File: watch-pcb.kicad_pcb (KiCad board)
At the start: 4 copper layers, 40 x 42 mm, 134 parts, among them J4 USB_C_Receptacle, J5 ESP_ANT, J6 GPS_ANT, Q1 BC818, U1 LIS3MDL, U10 MX25LM51245GXDI00, U11 LSM6DSV16XTR, U3 DRV2605LYZFR, U4 TPS63001, U5 AP131-18, U6 MAX30102, U7 MCP73871-2AA, U8 ESP32-S3, U9 S80KS5123GABHI020, Y1 40MHz(10ppm), Y2 32.768kHz

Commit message: custom symbols moar
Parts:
- moved U11 5.92 mm to (90.2, 104.8), turned to 0 degrees
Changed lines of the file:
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@@
   )
   (footprint "LSM6DSV16XTR:LGA14L_LSM6_STM" (layer "F.Cu")
-    (at 84.35 104.3 90)
+    (at 90.249811 104.8189)
     (tags "LSM6DSV16XTR ")
     (property "Sheetfile" "watch_pcb.kicad_sch")
@@
     (property "ki_keywords" "LSM6DSV16XTR")
     (attr smd)
-    (fp_text reference "U11" (at 0 2.550189 90 unlocked) (layer "F.SilkS")
-        (effects (font (size 1 1) (thickness 0.15)))
-    )
-    (fp_text value "LSM6DSV16XTR" (at 0 0 90 unlocked) (layer "F.Fab")
-        (effects (font (size 1 1) (thickness 0.15)))
-    )
-    (fp_text user "*" (at -2.0828 -0.750189 90 unlocked) (layer "F.SilkS")
-        (effects (font (size 1 1) (thickness 0.15)))
-    )
-    (fp_text user "*" (at -2.0828 -0.750189 90) (layer "F.SilkS")
-        (effects (font (size 1 1) (thickness 0.15)))
-    )
-    (fp_text user "*" (at -0.2794 -0.750189 90) (layer "F.Fab")
-        (effects (font (size 1 1) (thickness 0.15)))
-    )
-    (fp_text user "*" (at -0.2794 -0.750189 90 unlocked) (layer "F.Fab")
-        (effects (font (size 1 1) (thickness 0.15)))
-    )
-    (fp_text user "${REFERENCE}" (at 0 0 90 unlocked) (layer "F.Fab")
+    (fp_text reference "U11" (at 0 2.550189 unlocked) (layer "F.SilkS")
+        (effects (font (size 1 1) (thickness 0.15)))
+    )
+    (fp_text value "LSM6DSV16XTR" (at 0 0 unlocked) (layer "F.Fab")
+        (effects (font (size 1 1) (thickness 0.15)))
+    )
+    (fp_text user "*" (at -2.0828 -0.750189 unlocked) (layer "F.SilkS")
+        (effects (font (size 1 1) (thickness 0.15)))
+    )
+    (fp_text user "*" (at -2.0828 -0.750189) (layer "F.SilkS")
+        (effects (font (size 1 1) (thickness 0.15)))
+    )
+    (fp_text user "*" (at -0.2794 -0.750189) (layer "F.Fab")
+        (effects (font (size 1 1) (thickness 0.15)))
+    )
+    (fp_text user "*" (at -0.2794 -0.750189 unlocked) (layer "F.Fab")
+        (effects (font (size 1 1) (thickness 0.15)))
+    )
+    (fp_text user "${REFERENCE}" (at 0 0 unlocked) (layer "F.Fab")
         (effects (font (size 1 1) (thickness 0.15)))
     )
@@
     (fp_line (start 1.5494 1.2954) (end 1.5494 -1.2954)
       (stroke (width 0.0254) (type solid)) (layer "F.Fab"))
-    (pad "1" smd rect (at -1.1811 -0.750189 180) (size 0.3048 0.5334) (layers "F.Cu" "F.Paste" "F.Mask")
+    (pad "1" smd rect (at -1.1811 -0.750189 90) (size 0.3048 0.5334) (layers "F.Cu" "F.Paste" "F.Mask")
       (net 9 "GND") (pinfunction "SDO/SA0") (pintype "unspecified"))
-    (pad "2" smd rect (at -1.1811 -0.250063 180) (size 0.3048 0.5334) (layers "F.Cu" "F.Paste" "F.Mask")
+    (pad "2" smd rect (at -1.1811 -0.250063 90) (size 0.3048 0.5334) (layers "F.Cu" "F.Paste" "F.Mask")
       (net 4 "/IMU_SDA") (pinfunction "SDx/AH1/QVAR1") (pintype "unspecified"))
-    (pad "3" smd rect (at -1.1811 0.250063 180) (size 0.3048 0.5334) (layers "F.Cu" "F.Paste" "F.Mask")
+    (pad "3" smd rect (at -1.1811 0.250063 90) (size 0.3048 0.5334) (layers "F.Cu" "F.Paste" "F.Mask")
       (net 1 "/IMU_SCL") (pinfunction "SCx/AH2/QVAR2") (pintype "unspecified"))
-    (pad "4" smd rect (at -1.1811 0.750189 180) (size 0.3048 0.5334) (layers "F.Cu" "F.Paste" "F.Mask")
+    (pad "4" smd rect (at -1.1811 0.750189 90) (size 0.3048 0.5334) (layers "F.Cu" "F.Paste" "F.Mask")
       (net 50 "/IMU_Wakeup") (pinfunction "INT1") (pintype "input"))
-    (pad "5" smd rect (at -0.500126 0.9271 90) (size 0.3048 0.5334) (layers "F.Cu" "F.Paste" "F.Mask")
+    (pad "5" smd rect (at -0.500126 0.9271) (size 0.3048 0.5334) (layers "F.Cu" "F.Paste" "F.Mask")
       (net 10 "+3V3") (pinfunction "VDD_IO") (pintype "power_in"))
-    (pad "6" smd rect (at 0 0.9271 90) (size 0.3048 0.5334) (layers "F.Cu" "F.Paste" "F.Mask")
+    (pad "6" smd rect (at 0 0.9271) (size 0.3048 0.5334) (layers "F.Cu" "F.Paste" "F.Mask")
       (net 9 "GND") (pinfunction "GND") (pintype "power_out"))
-    (pad "7" smd rect (at 0.500126 0.9271 90) (size 0.3048 0.5334) (layers "F.Cu" "F.Paste" "F.Mask")
+    (pad "7" smd rect (at 0.500126 0.9271) (size 0.3048 0.5334) (layers "F.Cu" "F.Paste" "F.Mask")
       (net 9 "GND") (pinfunction "GND") (pintype "power_out"))
-    (pad "8" smd rect (at 1.1811 0.750189 180) (size 0.3048 0.5334) (layers "F.Cu" "F.Paste" "F.Mask")
+    (pad "8" smd rect (at 1.1811 0.750189 90) (size 0.3048 0.5334) (layers "F.Cu" "F.Paste" "F.Mask")
       (net 10 "+3V3") (pinfunction "VDD") (pintype "power_in"))
-    (pad "9" smd rect (at 1.1811 0.250063 180) (size 0.3048 0.5334) (layers "F.Cu" "F.Paste" "F.Mask")
+    (pad "9" smd rect (at 1.1811 0.250063 90) (size 0.3048 0.5334) (layers "F.Cu" "F.Paste" "F.Mask")
       (net 51 "/IMU_INT2") (pinfunction "INT2") (pintype "input"))
-    (pad "10" smd rect (at 1.1811 -0.250063 180) (size 0.3048 0.5334) (layers "F.Cu" "F.Paste" "F.Mask")
+    (pad "10" smd rect (at 1.1811 -0.250063 90) (size 0.3048 0.5334) (layers "F.Cu" "F.Paste" "F.Mask")
       (net 52 "unconnected-(U11-OCS_AUX-Pad10)") (pinfunction "OCS_AUX") (pintype "unspecified+no_connect"))
-    (pad "11" smd rect (at 1.1811 -0.750189 180) (size 0.3048 0.5334) (layers "F.Cu" "F.Paste" "F.Mask")
+    (pad "11" smd rect (at 1.1811 -0.750189 90) (size 0.3048 0.5334) (layers "F.Cu" "F.Paste" "F.Mask")
       (net 53 "unconnected-(U11-SDO_AUX-Pad11)") (pinfunction "SDO_AUX") (pintype "unspecified+no_connect"))
-    (pad "12" smd rect (at 0.500126 -0.9271 90) (size 0.3048 0.5334) (layers "F.Cu" "F.Paste" "F.Mask")
+    (pad "12" smd rect (at 0.500126 -0.9271) (size 0.3048 0.5334) (layers "F.Cu" "F.Paste" "F.Mask")
       (net 10 "+3V3") (pinfunction "CS") (pintype "unspecified"))
-    (pad "13" smd rect (at 0 -0.9271 90) (size 0.3048 0.5334) (layers "F.Cu" "F.Paste" "F.Mask")
+    (pad "13" smd rect (at 0 -0.9271) (size 0.3048 0.5334) (layers "F.Cu" "F.Paste" "F.Mask")
       (net 7 "/I2C0_SCL") (pinfunction "SCL") (pintype "unspecified"))
-    (pad "14" smd rect (at -0.500126 -0.9271 90) (size 0.3048 0.5334) (layers "F.Cu" "F.Paste" "F.Mask")
+    (pad "14" smd rect (at -0.500126 -0.9271) (size 0.3048 0.5334) (layers "F.Cu" "F.Paste" "F.Mask")
       (net 8 "/I2C0_SDA") (pinfunction "SDA") (pintype "unspecified"))
   )

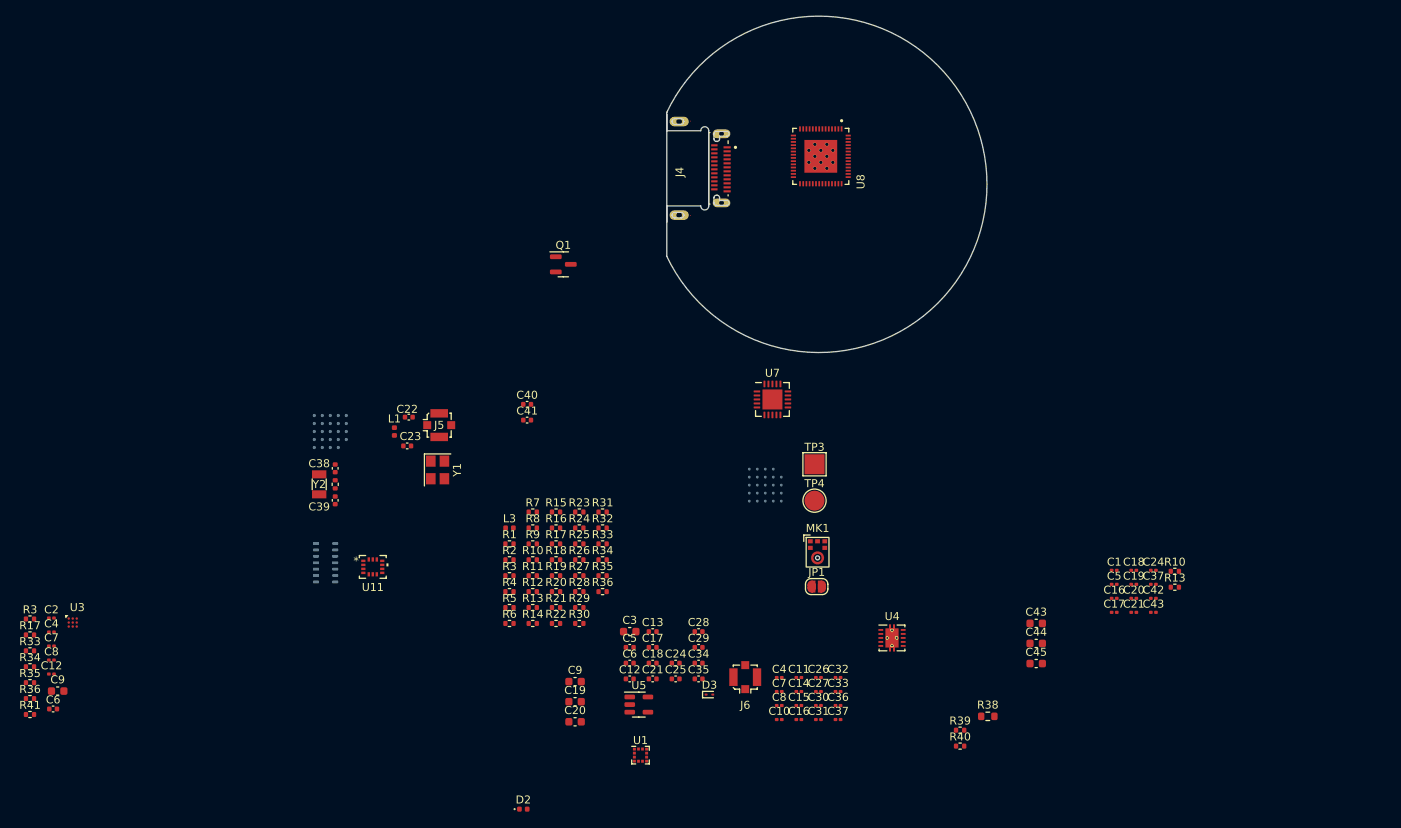
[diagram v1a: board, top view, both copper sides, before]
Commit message: finished schematic, verifying design and doing daughter board
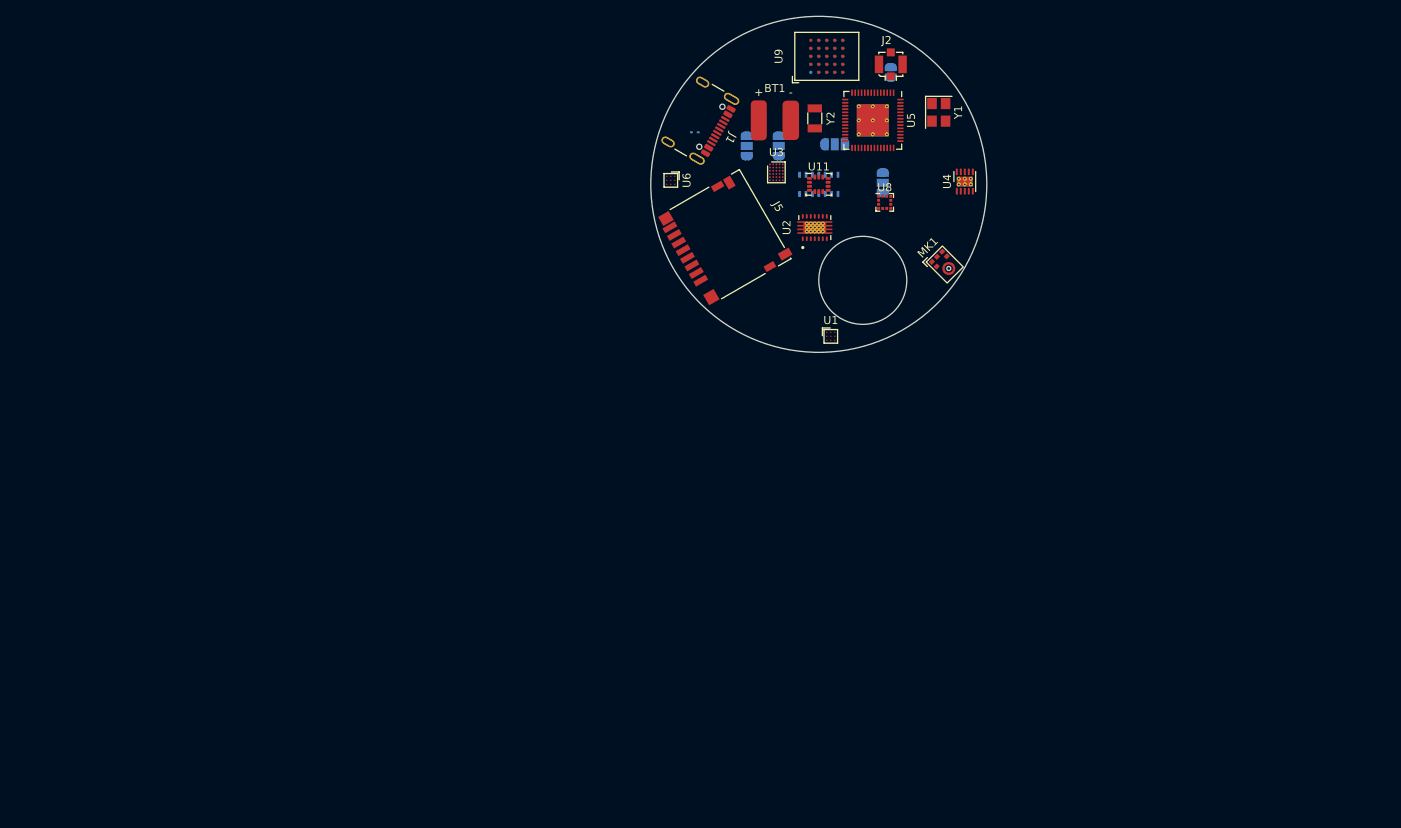
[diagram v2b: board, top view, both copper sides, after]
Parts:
- removed C1, C12, C17, C18, C4, C42, C5: 1uF, Capacitor_SMD:C_0201_0603Metric
- removed C10, C11, C15, C16 (x2), C2, C27, C30, C31, C32, C33, C36, C37, C4, C7 (x2), C8 (x2): 100nF, Capacitor_SMD:C_0201_0603Metric
- removed C12, C17, C25, C28, C29, C34: 1uF, Capacitor_SMD:C_0402_1005Metric
- removed C13, C18, C35, C5, C6 (x2): 10uF, Capacitor_SMD:C_0402_1005Metric
- removed C14, C26: 10nF, Capacitor_SMD:C_0201_0603Metric
- removed C19: 47nF, Capacitor_SMD:C_0201_0603Metric
- removed C19, C20, C9 (x2): 4.7uF, Capacitor_SMD:C_0603_1608Metric
- removed C20: 4.7uF, Capacitor_SMD:C_0201_0603Metric
- removed C21, C24, C37: 10uF, Capacitor_SMD:C_0201_0603Metric
- removed C21, C24, C38, C39, C40, C41: C, Capacitor_SMD:C_0402_1005Metric
- removed C22, C23: 1.5pF, Capacitor_SMD:C_0402_1005Metric
- removed C3: 1uF, Capacitor_SMD:C_0603_1608Metric
- removed C43: 2.2uF, Capacitor_SMD:C_0201_0603Metric
- removed C43, C44, C45: 10uF, Capacitor_SMD:C_0603_1608Metric
- removed D2: CHG_STATUS, LED_SMD:LED_0402_1005Metric
- removed D3: ESD9B5.0ST5G, Diode_SMD:D_SOD-923
- removed J4: USB_C_Receptacle, DX07B024JJ1R1500:JAE_DX07B024JJ1R1500
- removed J6: GPS_ANT, Connector_Coaxial:U.FL_Molex_MCRF_73412-0110_Vertical
- removed L1: 2.7nH, Inductor_SMD:L_0402_1005Metric
- removed L3: 2nH, Inductor_SMD:L_0402_1005Metric
- removed Q1: BC818, Package_TO_SOT_SMD:SOT-23
- removed R1, R2: 5.1k, Resistor_SMD:R_0402_1005Metric
- removed R10 (x2), R13, R17, R18, R19, R20, R3, R31, R32, R33, R34, R35, R36, R4, R41, R5, R6, R7, R8, R9: 10k, Resistor_SMD:R_0402_1005Metric
- removed R11: 100k, Resistor_SMD:R_0402_1005Metric
- removed R12, R33, R34: 2k, Resistor_SMD:R_0402_1005Metric
- removed R13: 50k, Resistor_SMD:R_0402_1005Metric
- removed R14: 470, Resistor_SMD:R_0402_1005Metric
- removed R15, R16, R3, R39: 1k, Resistor_SMD:R_0402_1005Metric
- removed R17, R21, R22, R23, R24, R25, R26, R27, R28, R29, R30: 0, Resistor_SMD:R_0402_1005Metric
- removed R35, R36, R37: R, Resistor_SMD:R_0402_1005Metric
- removed R38: 10, Resistor_SMD:R_0603_1608Metric
- removed R40: 100, Resistor_SMD:R_0402_1005Metric
- removed TP3: Conn_B-, TestPoint:TestPoint_Pad_2.5x2.5mm
- removed TP4: Conn_B+, TestPoint:TestPoint_Pad_D2.5mm
- added BT1: Battery, custom-lib:Battery_Connector, F.Cu at (140.5, 49.0)
- added D1: ESD9B5.0ST5G, Diode_SMD:D_SOD-923, B.Cu at (130.5, 50.5)
- added J1: USB_C_Receptacle, Connector_USB:USB_C_Receptacle_GCT_USB4105-xx-A_16P_TopMnt_Horizontal, F.Cu at (130.2, 48.5)
- added J2: ESP_ANT, Connector_Coaxial:U.FL_Molex_MCRF_73412-0110_Vertical, F.Cu at (155.0, 42.0)
- added JP2: GP6, Jumper:SolderJumper-3_P1.3mm_Open_RoundedPad1.0x1.5mm, B.Cu at (141.0, 52.2)
- added JP3: GP6, Jumper:SolderJumper-3_P1.3mm_Open_RoundedPad1.0x1.5mm, B.Cu at (148.0, 52.0)
- added JP4: GP6, Jumper:SolderJumper-3_P1.3mm_Open_RoundedPad1.0x1.5mm, B.Cu at (154.0, 56.8)
- added JP5: GP6, Jumper:SolderJumper-3_P1.3mm_Open_RoundedPad1.0x1.5mm, B.Cu at (137.0, 52.2)
- added U2: TPS63021, custom-lib:Texas_VSON-14_3x4mm_ThermalPad, F.Cu at (145.5, 62.4)
- J5: value ESP_ANT -> Micro_SD_Card; footprint Connector_Coaxial:U.FL_Molex_MCRF_73412-0110_Vertical -> Connector_Card:microSD_HC_Hirose_DM3D-SF
- JP1: moved to B.Cu
- U1: value LIS3MDL -> DRV2605LYZFR; footprint Package_LGA:LGA-12_2x2mm_P0.5mm -> Package_BGA:Texas_DSBGA-9_1.4715x1.4715mm_Layout3x3_P0.5mm
- U10: value MX25LM51245GXDI00 -> APS12808L-3OBMx; footprint MX25UM51245G:CSP24_6X8X1.2_MAC -> custom-lib:BGA-24_6.0x8.0mm_Layout5x5_P1.0mm
- U11: footprint LSM6DSV16XTR:LGA14L_LSM6_STM -> Package_LGA:LGA-14_3x2.5mm_P0.5mm_LayoutBorder3x4y
- U3: value DRV2605LYZFR -> BQ25638; footprint DRV2605L:YZF0009ADAD -> custom-lib:Texas_DSBGA-30_2.0x2.4mm_Layout5x6_P0.4mm
- U4: value TPS63001 -> TPS65631W; footprint Package_SON:Texas_DRC0010J_ThermalVias -> Package_SON:WSON-10-1EP_2.5x2.5mm_P0.5mm_EP1.2x2mm_ThermalVias
- U5: value AP131-18 -> ESP32-S3; footprint Package_TO_SOT_SMD:SOT-23-5 -> Package_DFN_QFN:QFN-56-1EP_7x7mm_P0.4mm_EP4x4mm_ThermalVias
- U6: value MAX30102 -> BQ27427YZFR; footprint OptoDevice:Maxim_OLGA-14_3.3x5.6mm_P0.8mm -> Package_BGA:Texas_DSBGA-9_1.4715x1.4715mm_Layout3x3_P0.5mm; moved to F.Cu
- U7: value MCP73871-2AA -> MAX30102; footprint Package_DFN_QFN:QFN-20-1EP_4x4mm_P0.5mm_EP2.5x2.5mm -> OptoDevice:Maxim_OLGA-14_3.3x5.6mm_P0.8mm; moved to B.Cu
- U8: value ESP32-S3 -> LIS3MDL; footprint ESP32-S3:IC_ESP32-S3 -> Package_LGA:LGA-12_2x2mm_P0.5mm
- U9: value S80KS5123GABHI020 -> MX25LM51245GXDI00; footprint S80KS5123GABHI020:PG-BGA-24-801 -> custom-lib:BGA-24_6.0x8.0mm_Layout5x5_P1.0mm; moved to F.Cu
- moved U3 104.4 mm to (140.7, 55.5)
- moved U5 78.7 mm to (152.8, 49.0), turned to -90 degrees
- moved U9 77.8 mm to (147.0, 41.0)
- moved Y2 77.0 mm to (145.5, 48.8)
- moved Y1 77.0 mm to (161.0, 48.0)
- moved U11 73.4 mm to (146.0, 57.0)
- moved JP1 64.9 mm to (155.0, 43.0), turned to -90 degrees
- moved U6 64.4 mm to (127.5, 56.5), turned to -90 degrees
- moved U4 57.8 mm to (164.2, 56.6), turned to 90 degrees
- moved U1 57.5 mm to (147.5, 76.0)
- moved U10 54.1 mm to (147.0, 41.0), turned to -90 degrees
- moved J5 42.8 mm to (134.3, 63.6), turned to -60 degrees
- moved MK1 39.3 mm to (161.7, 67.0), turned to 45 degrees
- moved U7 27.5 mm to (146.0, 57.0), turned to 90 degrees
- moved U8 9.84 mm to (154.2, 59.2), turned to 0 degrees
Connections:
- J5 pad 1: Net-(J5-In) -> /SD_D2
- J5 pad 2: GND -> /SD_D3
- U10 pad A3: unconnected-(U10-NC-PadA3) -> /MEM_CS1
- U10 pad A4: Net-(U10-RESET#) -> /RAM_RST
- U10 pad B4: VMEM -> +3V3
- U10 pad C2: /MEM_CS0 -> (no net)
- U10 pad D1: VMEM -> +3V3
- U10 pad E4: VMEM -> +3V3
- U11 pad 9: /IMU_INT2 -> unconnected-(U11-INT2-Pad9)
- U3 pad A1: +3V3 -> +5V
- U3 pad A2: Net-(U3-REG) -> Net-(C16-Pad2)
- U3 pad A3: /MTR_P -> Net-(C23-Pad2)
- U3 pad B1: GND -> +5V
- U3 pad B2: /I2C1_SDA -> Net-(C16-Pad2)
- U3 pad B3: GND -> Net-(C23-Pad2)
- U3 pad C1: /I2C1_SCL -> Net-(D2-K)
- U3 pad C2: +3V3 -> Net-(D3-K)
- U3 pad C3: /MTR_M -> Net-(C23-Pad2)
- U4 pad 1: +3V3 -> Net-(U4-SWP)
- U4 pad 2: Net-(U4-L2) -> GND
- U4 pad 3: GND -> /AMOLED_P
- U4 pad 4: Net-(U4-L1) -> /AMOLED_P
- U4 pad 5: +BATT -> GND
- U4 pad 6: Net-(U4-EN) -> /SWIRE
- U4 pad 7: Net-(U4-EN) -> /AMOLED_N
- U4 pad 8: Net-(U4-EN) -> Net-(U4-SWN)
- U4 pad 9: GND -> +3V3
- U5 pad 1: +BATT -> /ESP_ANT
- U5 pad 2: GND -> Net-(U5-VDD3P3)
- U5 pad 3: +BATT -> Net-(U5-VDD3P3)
- U5 pad 5: +1V8 -> /I2C0_SCL
- U7 pad 1: +BATT -> unconnected-(U7-NC-Pad1)
- U7 pad 10: GND -> +3V3
- U7 pad 11: GND -> +1V8
- U7 pad 12: Net-(U7-PROG3) -> GND
- U7 pad 13: Net-(U7-PROG1) -> /HBT_INT
- U7 pad 14: /BATT+ -> unconnected-(U7-NC-Pad14)
- U7 pad 2: +5V -> /IMU_SCL
- U7 pad 3: GND -> /IMU_SDA
- U7 pad 4: +5V -> GND
- U7 pad 5: Net-(U7-THERM) -> unconnected-(U7-NC-Pad5)
- U7 pad 6: Net-(U7-~{PG}) -> unconnected-(U7-NC-Pad6)
- U7 pad 7: /BAT_STAT2 -> unconnected-(U7-NC-Pad7)
- U7 pad 8: /BAT_STAT1 -> unconnected-(U7-NC-Pad8)
- U7 pad 9: GND -> +3V3
- U8 pad 1: /ESP_ANT -> /IMU_SCL
- U8 pad 10: /MIC_SCK -> +3V3
- U8 pad 11: /MIC_SD -> /IMU_SDA
- U8 pad 12: unconnected-(U8-GPIO7-Pad12) -> GND
- U8 pad 2: Net-(U8-VDD3P3) -> GND
- U8 pad 3: Net-(U8-VDD3P3) -> GND
- U8 pad 5: /I2C0_SCL -> +3V3
- U8 pad 6: /I2C0_SDA -> +3V3
- U8 pad 7: /I2C1_SCL -> /MAG_INT
- U8 pad 8: /I2C1_SDA -> unconnected-(U8-DRDY-Pad8)
- U8 pad 9: /MIC_WS -> GND
- U9 pad A3: /MEM_CS1 -> unconnected-(U9-NC-PadA3)
- U9 pad A4: Net-(U9-RESET#) -> /FLASH_RST
- U9 pad A5: unconnected-(U9-RFU-PadA5) -> /FLASH_ECS
- U9 pad B1: GND -> unconnected-(U9-DNU-PadB1)
- U9 pad B4: VMEM -> +3V3
- U9 pad C2: unconnected-(U9-RFU-PadC2) -> /MEM_CS0
- U9 pad D1: VMEM -> +3V3
- U9 pad E4: VMEM -> +3V3
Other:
- board size 40 x 42 mm -> 42 x 42 mm

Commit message: nearly done with schematic i thinks
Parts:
- added C70: 1.5pF, Capacitor_SMD:C_0201_0603Metric, F.Cu at (199.5, 43.4)
- added C71: 1.5pF, Capacitor_SMD:C_0201_0603Metric, F.Cu at (199.5, 45.1)
- added D4: ESD9B3.3ST5G, Diode_SMD:D_SOD-923, F.Cu at (199.1, 56.0)
- added D5: ESD9B3.3ST5G, Diode_SMD:D_SOD-923, F.Cu at (199.1, 58.0)
- added J4: MOTOR, custom-lib:Battery_Connector, F.Cu at (194.8, 45.5)
- added J6: ESP_ANT, Connector_Coaxial:U.FL_Molex_MCRF_73412-0110_Vertical, F.Cu at (185.0, 54.8)
- added JP6: RESET=LOW, Jumper:SolderJumper-2_P1.3mm_Open_RoundedPad1.0x1.5mm, F.Cu at (195.5, 56.9)
- added JP8: GP6, Jumper:SolderJumper-3_P1.3mm_Open_RoundedPad1.0x1.5mm, F.Cu at (184.8, 59.5)
- added L7: 2.7nH, Inductor_SMD:L_0201_0603Metric, F.Cu at (199.5, 46.9)
- added R21: R, PCM_Resistor_SMD_AKL:R_0402_1005Metric, F.Cu at (194.8, 59.7)
- added U12: ESP32-S3, Package_DFN_QFN:QFN-56-1EP_7x7mm_P0.4mm_EP4x4mm_ThermalVias, F.Cu at (186.6, 47.1)
- added U13: ADP2108AUJ-1.8, Package_TO_SOT_SMD:TSOT-23-5, F.Cu at (190.6, 58.4)
- added Y3: 40MHz(10ppm), Crystal:Crystal_SMD_3225-4Pin_3.2x2.5mm, F.Cu at (190.7, 54.0)
- added Y4: 32.768kHz, Crystal:Crystal_SMD_3215-2Pin_3.2x1.5mm, F.Cu at (195.8, 53.4)
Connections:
- U1 pad B2: /I2C1_SDA -> /I2C0_SDA
- U1 pad C1: /I2C1_SCL -> /I2C0_SCL
- U10 pad A4: /RAM_RST -> Net-(U10-RST#)
- U11 pad 13: /I2C0_SCL -> /I2C1_SCL
- U11 pad 14: /I2C0_SDA -> /I2C1_SDA
- U3 pad D5: /I2C1_SCL -> /I2C0_SCL
- U3 pad E5: /I2C1_SDA -> /I2C0_SDA
- U6 pad A2: /I2C1_SDA -> /I2C0_SDA
- U6 pad A3: /I2C1_SCL -> /I2C0_SCL
- U9 pad A4: /FLASH_RST -> Net-(U9-RESET#)
- U9 pad A5: /FLASH_ECS -> Net-(U9-ECS#)

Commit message: basically done probably
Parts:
- added BT2: Battery, custom-lib:Battery_Connector, F.Cu at (201.0, 82.8)
- added C100: 1.5pF, Capacitor_SMD:C_0201_0603Metric, F.Cu at (193.8, 70.7)
- added C102: 1.5pF, Capacitor_SMD:C_0201_0603Metric, F.Cu at (193.8, 72.4)
- added D1: ESD9B5.0ST5G, Diode_SMD:D_SOD-923, F.Cu at (211.7, 80.8)
- added D2: ESD9B5.0ST5G, Diode_SMD:D_SOD-923, F.Cu at (211.7, 82.7)
- added D3: ESD9B5.0ST5G, Diode_SMD:D_SOD-923, F.Cu at (211.7, 84.7)
- added D9: ESD9B5.0ST5G, Diode_SMD:D_SOD-923, F.Cu at (211.7, 86.6)
- added J1: ESP_ANT, Connector_Coaxial:U.FL_Molex_MCRF_73412-0110_Vertical, F.Cu at (189.5, 72.8)
- added J2: MOTOR, custom-lib:Battery_Connector, F.Cu at (205.8, 95.2)
- added J5: Micro_SD_Card, Connector_Card:microSD_HC_Hirose_DM3D-SF, F.Cu at (176.7, 87.9)
- added J7: USB_C_Receptacle, Connector_USB:USB_C_Receptacle_GCT_USB4105-xx-A_16P_TopMnt_Horizontal, F.Cu at (203.3, 75.1)
- added JP7: RESET=LOW, Jumper:SolderJumper-2_P1.3mm_Open_RoundedPad1.0x1.5mm, F.Cu at (192.6, 94.8)
- added L13: 2.7nH, Inductor_SMD:L_0201_0603Metric, F.Cu at (193.8, 74.2)
- added MK1: ICS-43434, Sensor_Audio:InvenSense_ICS-43434-6_3.5x2.65mm, F.Cu at (204.6, 101.0)
- added MK2: ICS-43434, Sensor_Audio:InvenSense_ICS-43434-6_3.5x2.65mm, F.Cu at (209.0, 101.0)
- added Q1: MBT2222ADW1T1, Package_TO_SOT_SMD:SOT-363_SC-70-6, F.Cu at (206.6, 88.3)
- added R57: R, PCM_Resistor_SMD_AKL:R_0402_1005Metric, F.Cu at (193.3, 76.9)
- added U1: DRV2605LYZFR, Package_BGA:Texas_DSBGA-9_1.4715x1.4715mm_Layout3x3_P0.5mm, F.Cu at (199.7, 101.7)
- added U10: APS12808L-3OBMx, custom-lib:BGA-24_6.0x8.0mm_Layout5x5_P1.0mm, F.Cu at (182.2, 75.1)
- added U11: LSM6DSV16XTR, Package_LGA:LGA-14_3x2.5mm_P0.5mm_LayoutBorder3x4y, F.Cu at (204.6, 105.5)
- added U14: CP2102N-Axx-xQFN28, Package_DFN_QFN:QFN-28-1EP_5x5mm_P0.5mm_EP3.35x3.35mm, F.Cu at (212.8, 73.4)
- added U16: BQ25638, custom-lib:Texas_DSBGA-30_2.0x2.4mm_Layout5x6_P0.4mm, F.Cu at (215.0, 86.6)
- added U17: ADP2108AUJ-1.8, Package_TO_SOT_SMD:TSOT-23-5, F.Cu at (200.1, 88.0)
- added U2: ESP32-S3, Package_DFN_QFN:QFN-56-1EP_7x7mm_P0.4mm_EP4x4mm_ThermalVias, F.Cu at (188.8, 85.0)
- added U3: TPS63021, custom-lib:Texas_VSON-14_3x4mm_ThermalPad, F.Cu at (207.7, 83.1)
- added U4: TPS65631W, Package_SON:WSON-10-1EP_2.5x2.5mm_P0.5mm_EP1.2x2mm_ThermalVias, F.Cu at (209.3, 105.5)
- added U5: BQ27427YZFR, Package_BGA:Texas_DSBGA-9_1.4715x1.4715mm_Layout3x3_P0.5mm, F.Cu at (215.2, 82.1)
- added U6: TCA9535MRGER, Package_DFN_QFN:VQFN-24-1EP_4x4mm_P0.5mm_EP2.45x2.45mm, F.Cu at (187.3, 92.8)
- added U7: MAX30102, OptoDevice:Maxim_OLGA-14_3.3x5.6mm_P0.8mm, F.Cu at (199.9, 95.8)
- added U8: LIS3MDL, Package_LGA:LGA-12_2x2mm_P0.5mm, F.Cu at (199.3, 105.7)
- added U9: MX25LM51245GXDI00, custom-lib:BGA-24_6.0x8.0mm_Layout5x5_P1.0mm, F.Cu at (173.6, 75.1)
- added Y5: 40MHz(10ppm), Crystal:Crystal_SMD_3225-4Pin_3.2x2.5mm, F.Cu at (189.1, 78.1)
- added Y6: 32.768kHz, Crystal:Crystal_SMD_3215-2Pin_3.2x1.5mm, F.Cu at (193.0, 91.3)
